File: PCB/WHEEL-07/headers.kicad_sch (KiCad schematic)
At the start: 34 parts, among them IC4 NL27WZ14DTT1G, J10 BUTTON, J12 Conn_01x10, J14 BUTTON, J15 BUTTON, J16 POWER, J17 TIM, J2 Conn_01x06_Male, J5 Conn_01x04_Male, J7 BUTTON, J8 BUTTON, J9 BUTTON

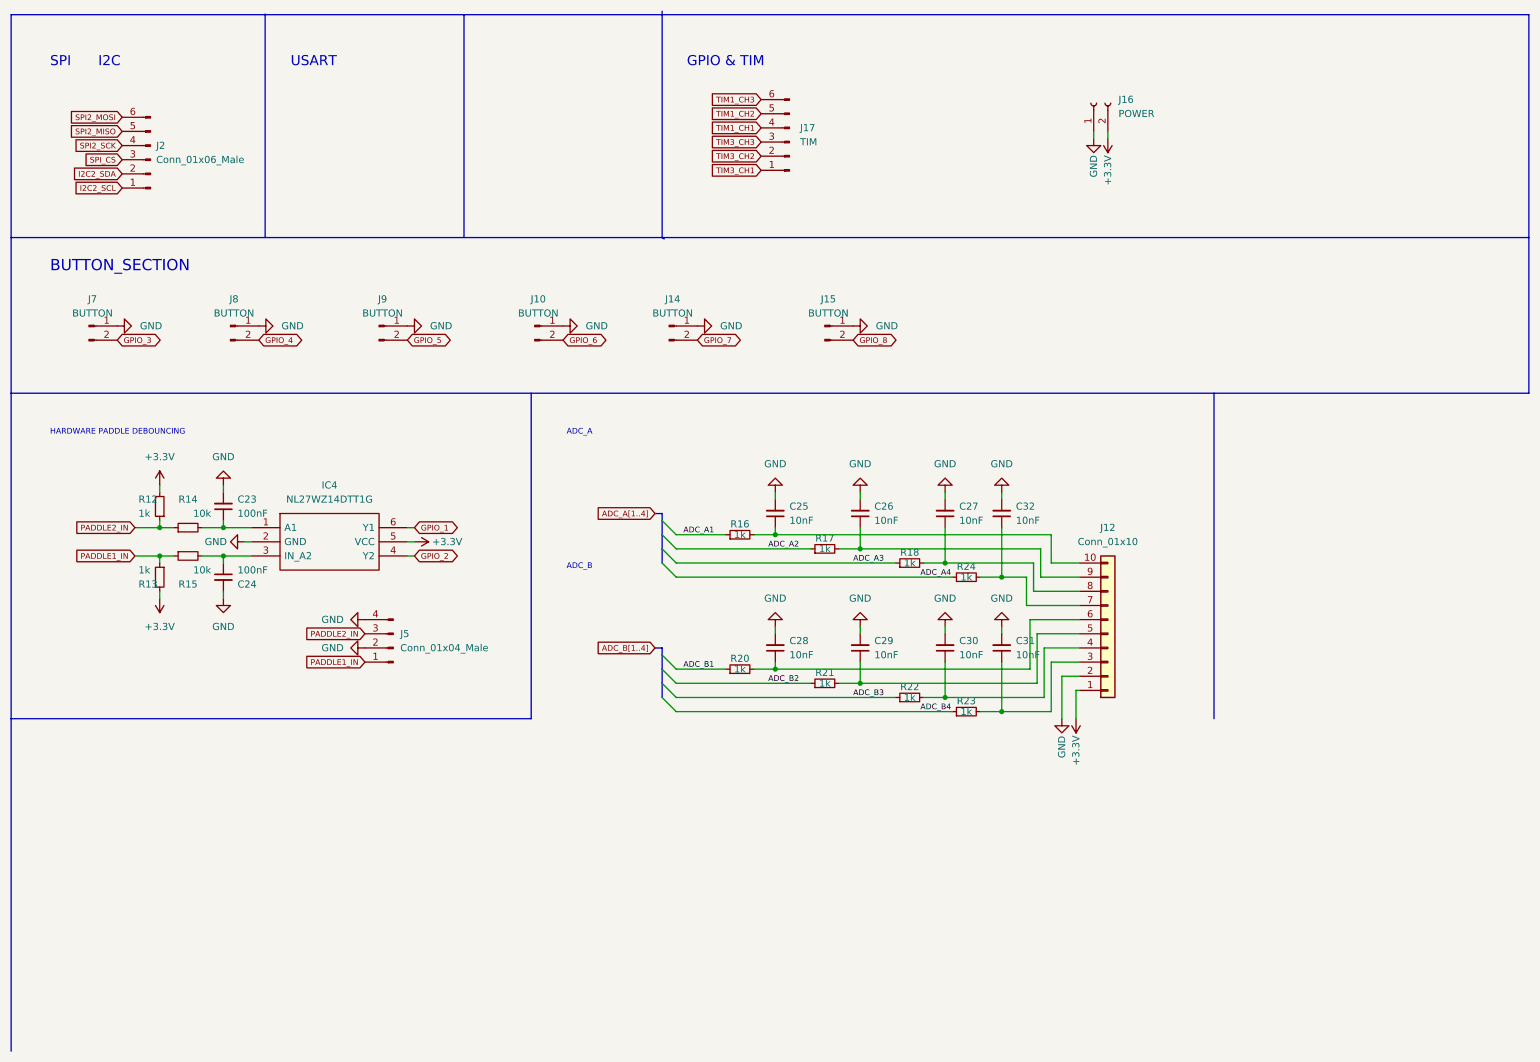
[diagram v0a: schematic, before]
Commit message: Revised board with 2 x LDO40 and cleaned-up schematics
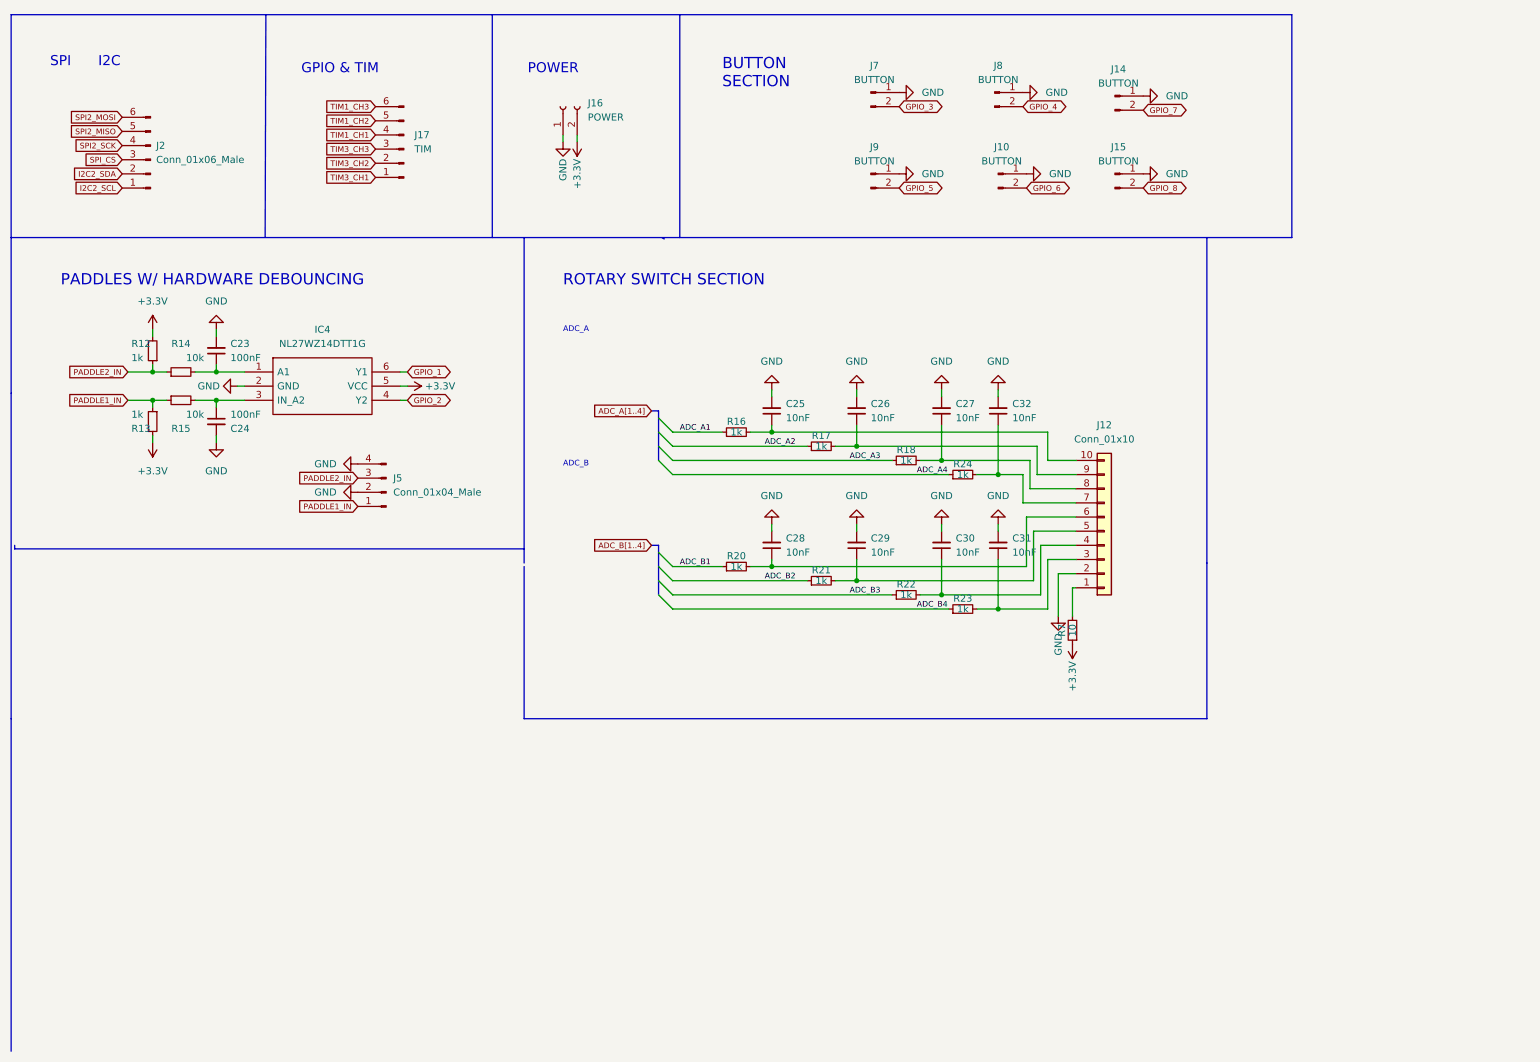
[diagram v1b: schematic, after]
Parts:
- added R7: 10, Resistor_SMD:R_0805_2012Metric, symbol Device:R_Small
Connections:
- net +3.3V: now also R7.1; no longer J12.1 (Pin_1)
- new net: J12.1 (Pin_1), R7.2
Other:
- note added: "BUTTON SECTION"
- note added: "PADDLES W/ HARDWARE DEBOUNCING"
- note added: "POWER"
- note added: "ROTARY SWITCH SECTION"
- note removed: "BUTTON_SECTION"
- note removed: "HARDWARE PADDLE DEBOUNCING"
- note removed: "USART"
- moved on the sheet: C23, C24, C25, C26, C27, C28, C29, C30, C31, C32, IC4, J10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
